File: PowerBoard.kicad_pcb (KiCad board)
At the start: 2 copper layers, 185 parts, among them J1 Conn_01x02_Socket, Q1 Q_NMOS, Q19 PSMN020-100YS, Q2 Q_NMOS, Q9 PSMN020-100YS, U10 LM5050-1, U11 TLV75533PDBV, U12 LT8640SEV_PBF, U13 TPS16851VMAR, U14 LM5050-1, U15 TPS26400PWP, U16 TPS26400PWP, U2 AD5259BRMZ100, U6 AD5259BRMZ100, U8 BNO055, U9 TPS16851VMAR

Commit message: Powerboard planning layout
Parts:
- added L1: 33uH, _PowerBoard:IND_XGL1313_COC-L, F.Cu at (115.4, 72.6)
- added L3: 33uH, _PowerBoard:IND_XGL1313_COC-L, F.Cu at (114.8, 110.6)
- added L4: 1.5uH, Inductor_SMD:Untitled, F.Cu at (149.8, 120.5)
- added U1: LT8342RV-TRMPBF, _PowerBoard:05-08-7040_ADI, F.Cu at (109.2, 60.9)
- added U3: RP2350A, _PowerBoard:QFN-60_7X7_RPI, B.Cu at (162.1, 42.2)
- added U4: LT8342RV-TRMPBF, _PowerBoard:05-08-7040_ADI, F.Cu at (109.2, 99.1)
- added U5: PINA745AIRELR, _PowerBoard:REL0014A_PINA745AIRELR_TEX, F.Cu at (99.8, 117.5)
- added U7: PINA745AIRELR, _PowerBoard:REL0014A_PINA745AIRELR_TEX, F.Cu at (146.2, 98.8)
- added X1: ABM8-272-T3, _PowerBoard:ABM8-272-T3_ABR, B.Cu at (169.7, 51.8)
- C19, C20, C21, C22, C23, C24, C27, C28, C29, C30, C31, C32, C33, C34: footprint Capacitor_SMD:C_0402_1005Metric -> Capacitor_SMD:C_0603_1608Metric; moved to B.Cu
- C25, C26: footprint Resistor_SMD:R_0201_0603Metric -> Capacitor_SMD:C_0603_1608Metric; moved to B.Cu
- L2: moved to B.Cu
- R10, R11, R13, R16, R9: footprint Resistor_SMD:R_0402_1005Metric -> Resistor_SMD:R_0603_1608Metric; moved to B.Cu
- R12, R14, R15, R7, R8: footprint Resistor_SMD:R_0201_0603Metric -> Resistor_SMD:R_0603_1608Metric; moved to B.Cu
- moved C51 176.1 mm to (147.5, 101.8), turned to 180 degrees
- moved TP2 175.7 mm to (154.4, 65.0)
- moved TP3 175.6 mm to (154.4, 72.8)
- moved TP6 174.8 mm to (155.8, 97.5)
- moved TP5 174.6 mm to (155.7, 89.3)
- moved C54 131.0 mm to (101.0, 120.6), turned to 180 degrees
- moved J1 116.3 mm to (169.6, 32.5)
- moved C20 109.0 mm to (167.8, 40.3)
- moved C19 108.9 mm to (167.8, 38.7)
- moved C21 108.1 mm to (167.8, 45.0)
- moved C29 106.5 mm to (165.0, 37.1)
- moved C22 105.7 mm to (165.6, 48.0), turned to -90 degrees
- moved R13 105.5 mm to (168.3, 37.0)
- moved C23 104.8 mm to (163.9, 48.0), turned to -90 degrees
- moved R14 103.4 mm to (165.8, 34.5), turned to 90 degrees
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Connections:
- Q1 pad 1: (no net) -> /Main/boost_a_frontend/GATE
- Q1 pad 2: (no net) -> Net-(L1-Pad1)
- Q1 pad 3: (no net) -> Net-(U1-SNS)
- Q2 pad 1: (no net) -> /Main/boost_b_frontend/GATE
- Q2 pad 2: (no net) -> Net-(Q2-S)
- Q2 pad 3: (no net) -> Net-(Q2-D)
- R20 pad 2: Net-(U4-SNS) -> Net-(Q2-D)
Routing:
- net +5V: track 12.3 -> 0.00 mm
- net Net-(U6-B): track 9.38 -> 0.00 mm
- net Net-(U2-B): track 9.38 -> 0.00 mm
- net Net-(U6-A): track 8.30 -> 0.00 mm
- net Net-(U2-A): track 8.30 -> 0.00 mm
- net Net-(U13-ILIM): track 6.47 -> 2.02 mm
- net /Main/navlight_load_sw1/IMON: track 4.09 -> 0.00 mm
- net /Main/batt2_lsw/IMON: track 3.99 -> 0.00 mm
- net +1V1: track 0.00 -> 3.39 mm
- net Net-(U13-IREF): track 2.95 -> 0.00 mm
- net Net-(U13-SFT_SEL): track 2.71 -> 0.00 mm
- net Net-(U16-dVdT): track 2.38 -> 0.00 mm
- net Net-(U13-dVdT): track 1.62 -> 0.00 mm
- net Net-(U16-MODE): track 1.30 -> 0.00 mm
- net /Main/navlight_load_sw1/nFLT: track 1.28 -> 0.00 mm
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- removed copper zone on F.Cu, net /Main/batt2_lsw/BUS
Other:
- board outline added: 100 x 60 mm

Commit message: Working on layout
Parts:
- removed TP2, TP5: TP_PGOOD, TestPoint:TestPoint_Plated_Hole_D5.0mm
- removed TP3, TP6: TP_FLTn, TestPoint:TestPoint_Plated_Hole_D5.0mm
- C17, C18, C38, C4, C52, C53, R1, R17, R18, R19, R2, R21, R22, R3, R5, R6, U2, U6: moved to B.Cu
- R20, R4: value R_US -> 3mOhm; footprint Resistor_SMD:R_0603_1608Metric -> Resistor_SMD:R_2512_6332Metric_Pad1.40x3.35mm_HandSolder
- moved C67 82.6 mm to (166.4, 113.9)
- moved D9 82.6 mm to (175.5, 115.4)
- moved C71 82.6 mm to (173.3, 114.7)
- moved U11 82.6 mm to (170.2, 114.7)
- moved C88 70.3 mm to (152.8, 129.0), turned to 180 degrees
- moved U16 67.7 mm to (154.8, 125.5), turned to 90 degrees
- moved R77 67.1 mm to (155.8, 121.5), turned to -90 degrees
- moved R74 66.1 mm to (155.8, 129.5), turned to 90 degrees
- moved C89 64.3 mm to (157.8, 121.5), turned to 90 degrees
- moved R75 63.5 mm to (157.8, 125.5), turned to 90 degrees
- moved R76 63.2 mm to (157.8, 129.5), turned to -90 degrees
- moved C55 60.0 mm to (191.9, 115.7)
- moved C56 60.0 mm to (191.9, 114.0)
- moved C57 60.0 mm to (195.8, 119.0)
- moved R23 60.0 mm to (201.2, 113.0)
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
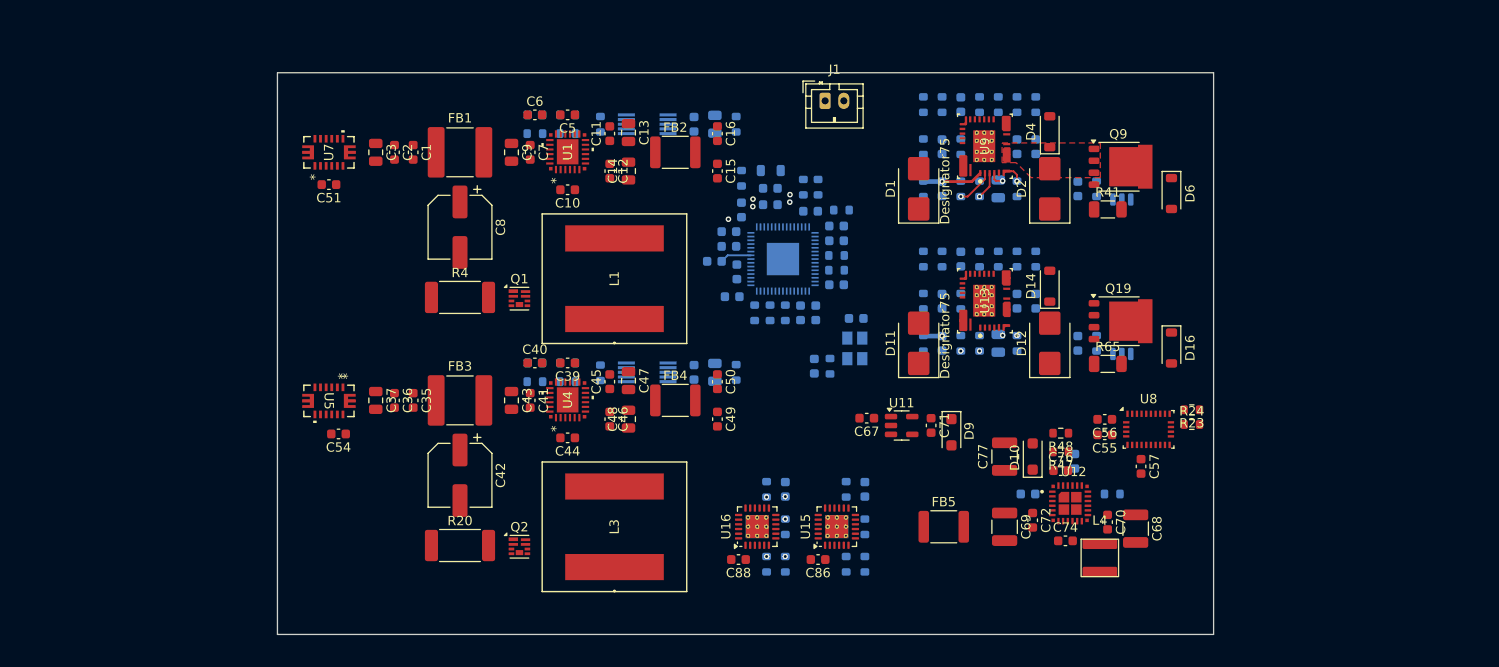
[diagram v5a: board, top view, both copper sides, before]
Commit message: Power board prelim routing
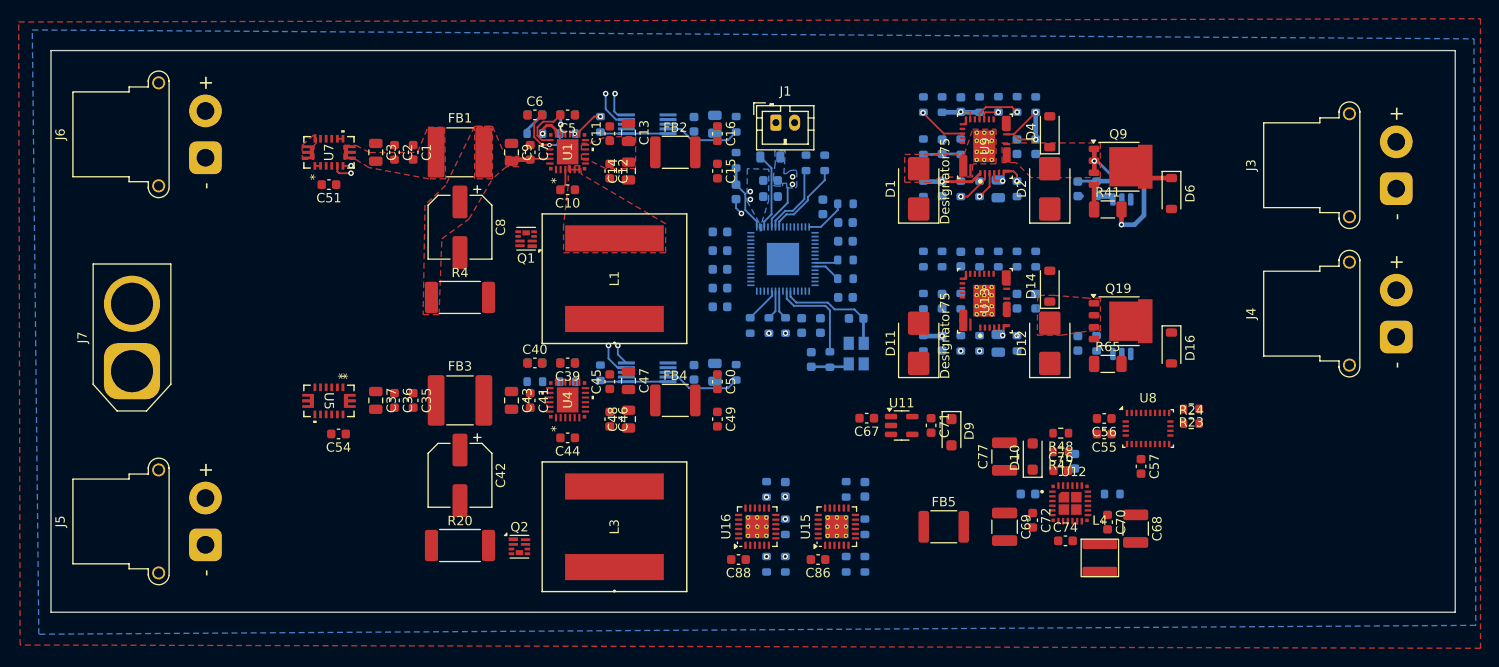
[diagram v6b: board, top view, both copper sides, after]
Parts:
- added J3: Conn_01x02_Pin, Connector_AMASS:AMASS_XT30PW-F_1x02_P2.50mm_Horizontal, F.Cu at (223.0, 89.4)
- added J4: Conn_01x02_Pin, Connector_AMASS:AMASS_XT30PW-F_1x02_P2.50mm_Horizontal, F.Cu at (223.0, 105.2)
- added J5: Conn_01x02_Pin, Connector_AMASS:AMASS_XT30PW-F_1x02_P2.50mm_Horizontal, F.Cu at (95.8, 127.4)
- added J6: Conn_01x02_Pin, Connector_AMASS:AMASS_XT30PW-F_1x02_P2.50mm_Horizontal, F.Cu at (95.8, 86.1)
- added J7: Conn_01x02_Socket, Connector_AMASS:AMASS_XT60-F_1x02_P7.20mm_Vertical, F.Cu at (88.0, 108.9)
- moved Q1 6.44 mm to (130.1, 94.7), turned to 180 degrees
- moved J1 5.75 mm to (156.7, 82.3)
- moved R14 2.69 mm to (162.0, 86.6)
- moved R15 2.61 mm to (160.0, 86.6)
- moved C33 2.59 mm to (156.2, 88.5)
- moved C27 2.50 mm to (150.8, 100.0), turned to 0 degrees
- moved C61 2.01 mm to (182.5, 80.4)
- moved R16 2.01 mm to (152.5, 86.3)
- moved C32 2.01 mm to (152.5, 89.7)
- moved R34 1.99 mm to (180.5, 80.4)
- moved C24 1.69 mm to (150.8, 102.0)
- moved C21 1.65 mm to (164.2, 101.0)
- moved L2 1.45 mm to (156.1, 86.0)
- moved C22 1.44 mm to (161.5, 104.0)
- moved R11 1.44 mm to (154.0, 104.0)
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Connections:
- J1 pad 1: unconnected-(J1-Pin_1-Pad1) -> /Main/mcu/SWDIO
- J1 pad 2: unconnected-(J1-Pin_2-Pad2) -> /Main/mcu/SWCLK
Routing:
- net /Main/SDA: track 0.00 -> 68.9 mm, vias 0 -> 3
- net /Main/SCL: track 0.00 -> 66.4 mm, vias 0 -> 3
- net /Main/mcu/SWCLK: track 0.00 -> 23.0 mm, vias 0 -> 1
- net /Main/mcu/SWDIO: track 0.00 -> 22.8 mm, vias 0 -> 1
- net Net-(U10-GATE): track 0.00 -> 13.4 mm, vias 0 -> 1
- net /Main/mcu/XIN: track 0.00 -> 12.0 mm
- net /Main/mcu/XOUT: track 0.00 -> 10.4 mm
- net Net-(U9-VDD): track 0.00 -> 9.55 mm, vias 0 -> 2
- net /Main/mcu/D+: track 0.00 -> 8.50 mm
- net Net-(U3-VREG_LX): track 0.00 -> 8.29 mm
- net Net-(U6-B): track 0.00 -> 8.13 mm
- net Net-(U2-B): track 0.00 -> 8.13 mm
- net /Main/mcu/D-: track 0.00 -> 7.83 mm
- net /Main/batt1_lsw/OUT: track 0.00 -> 7.38 mm
- net Net-(U2-A): track 0.00 -> 7.30 mm
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- added copper zone on B.Cu, net +1V1
- added copper zone on F.Cu, net /Main/batt2_lsw/BUS
- added copper zone on F.Cu, net /Main/boost_a_frontend/PANEL_IN
- added copper zone on F.Cu, net /Main/boost_a_frontend/Vout
- added copper zone on F.Cu, net /Main/boost_a_in_sns/IN
- added copper zone on B.Cu, net GND
- added copper zone on F.Cu, net GND
- added copper zone on In4.Cu, net GND
- added copper zone on F.Cu, net Net-(C10-Pad1)
- added copper zone on F.Cu, net Net-(U1-VIN)
- added copper zone on F.Cu, net VBUS
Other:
- board size 100 x 60 mm -> 150 x 60 mm
- copper layers 2 -> 6

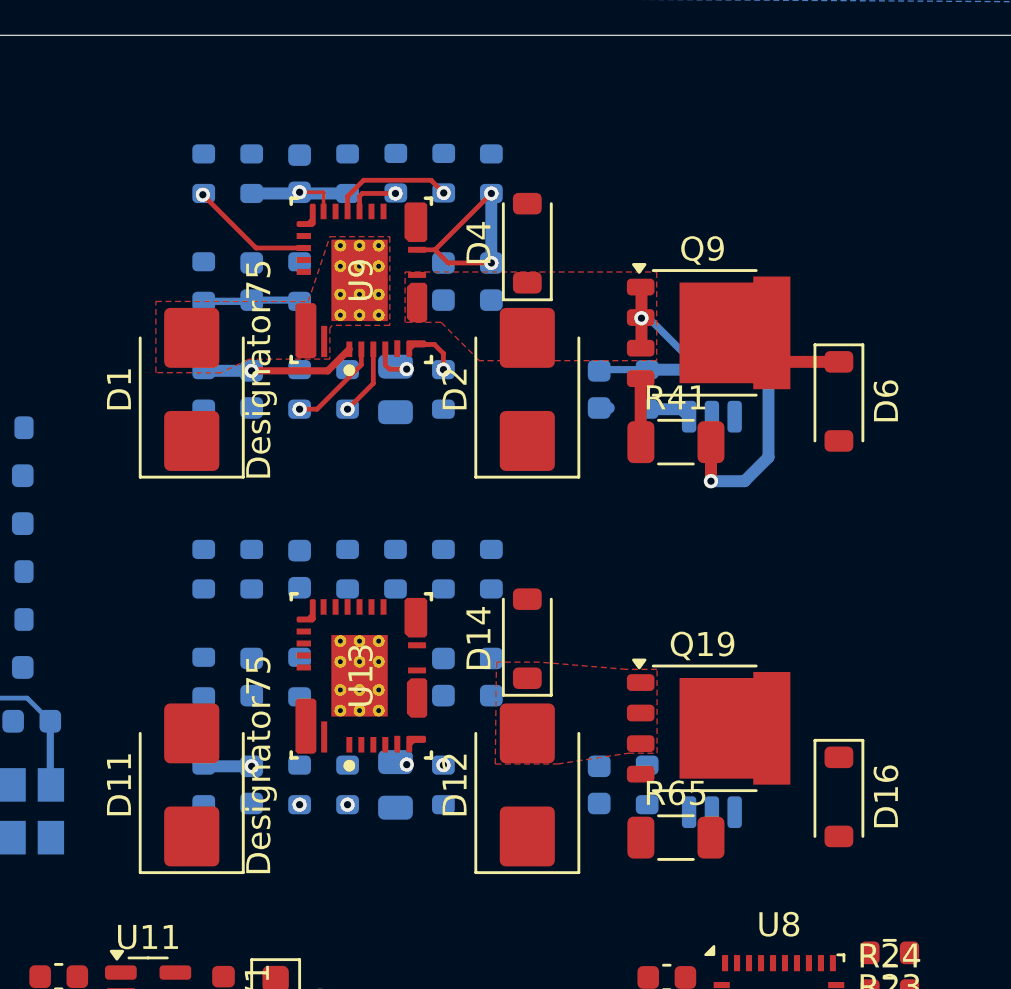
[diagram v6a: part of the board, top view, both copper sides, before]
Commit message: Touching up load switch
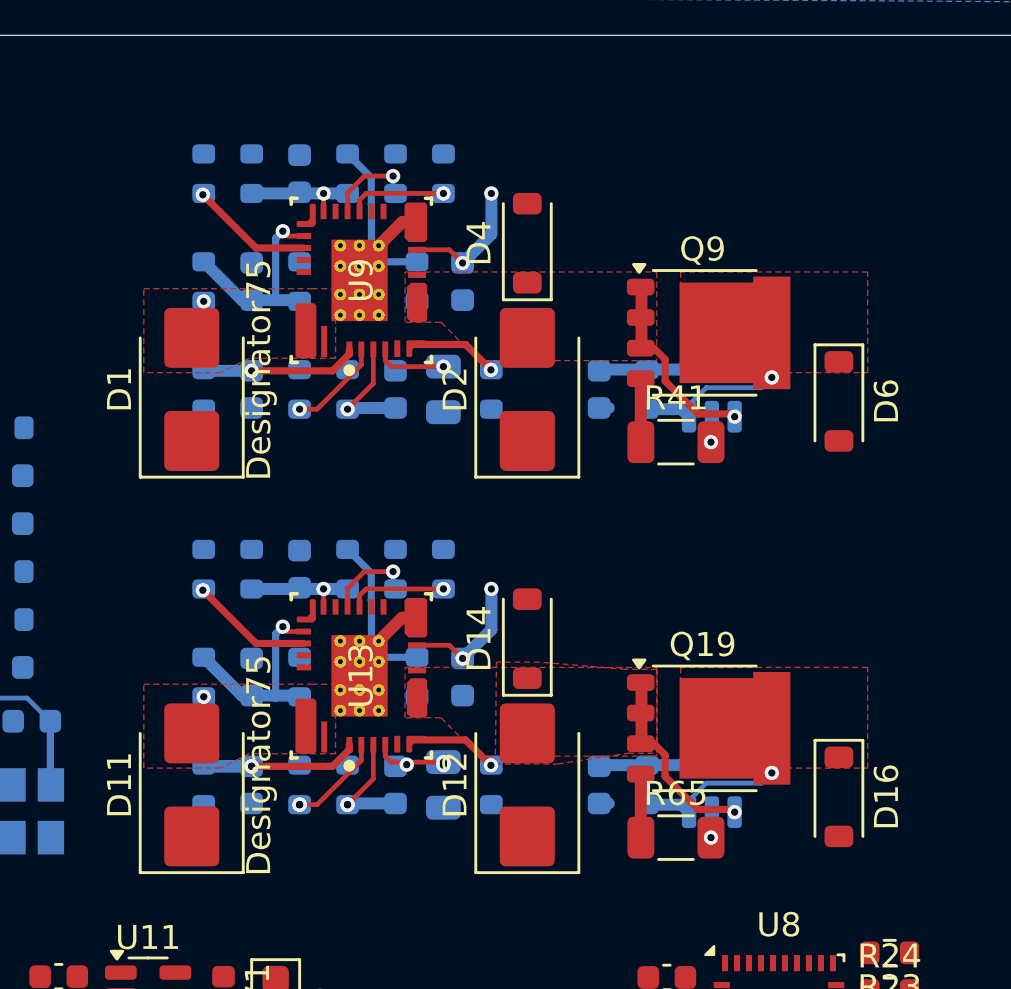
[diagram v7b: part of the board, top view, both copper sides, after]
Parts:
- moved R31 5.46 mm to (181.4, 84.9)
- moved R55 5.46 mm to (181.4, 101.4)
- moved C63 4.92 mm to (180.5, 89.4)
- moved C83 4.92 mm to (180.5, 105.9)
- moved C61 2.01 mm to (180.5, 80.4)
- moved C64 2.00 mm to (182.5, 89.4)
- moved C84 2.00 mm to (182.5, 105.9)
- moved R32 2.00 mm to (184.5, 89.4)
- moved R56 2.00 mm to (184.5, 105.9)
- moved R34 1.99 mm to (182.5, 80.4)
- moved C60 1.20 mm to (183.3, 84.9)
- moved C80 1.20 mm to (183.3, 101.4)
- turned C85 to -90 degrees
- turned R27 to 90 degrees
- turned R51 to 90 degrees
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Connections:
- U9 pad 25: (no net) -> VBUS
- U9 pad 26: (no net) -> VBUS
- U9 pad 27: (no net) -> VBUS
- U9 pad 28: (no net) -> VBUS
- U9 pad 29: (no net) -> VBUS
- U9 pad 30: (no net) -> VBUS
- U9 pad 31: (no net) -> VBUS
- U9 pad 32: (no net) -> VBUS
- U9 pad 33: (no net) -> VBUS
- U9 pad 34: (no net) -> VBUS
- U9 pad 35: (no net) -> VBUS
- U9 pad 36: (no net) -> VBUS
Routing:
- net VBUS: track 0.00 -> 15.5 mm, vias 0 -> 2
- net Net-(U10-GATE): track 13.4 -> 1.13 mm
- net Net-(U13-OVP): track 0.00 -> 8.71 mm, vias 0 -> 1
- net /Main/batt2_lsw/BUS: track 0.00 -> 8.21 mm, vias 0 -> 1
- net /Main/batt2_lsw/OUT: track 0.00 -> 8.01 mm, vias 0 -> 1
- net Net-(U13-ILIM): track 2.02 -> 8.61 mm, vias 1 -> 2
- net Net-(U13-VDD): track 0.00 -> 5.52 mm, vias 0 -> 2
- net /Main/batt2_lsw/PGOOD: track 0.00 -> 5.20 mm, vias 0 -> 1
- net Net-(U13-IREF): track 0.00 -> 4.97 mm, vias 1 -> 2
- net /Main/batt2_lsw/EN_UVLO: track 0.00 -> 4.75 mm, vias 0 -> 1
- net Net-(U9-OVP): track 4.04 -> 8.71 mm, vias 0 -> 1
- net /Main/batt2_lsw/FLTn: track 0.00 -> 4.09 mm, vias 0 -> 1
- net Net-(U9-VDD): track 9.55 -> 5.52 mm
- net /Main/batt2_lsw/IMON: track 0.00 -> 3.99 mm, vias 1 -> 2
- net Net-(U14-VS): track 0.00 -> 3.90 mm
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- added copper zone on F.Cu, net /Main/batt1_lsw/OUT
- added copper zone on F.Cu, net /Main/batt2_lsw/OUT
- added copper zone on F.Cu, net Net-(U13-IREF)
